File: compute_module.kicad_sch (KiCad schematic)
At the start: 4 parts

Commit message: Added annotated reference numbers
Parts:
- gave numbers to parts that had none: 4
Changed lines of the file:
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@@
   (symbol (lib_id "power:+3.3V") (at 195.58 60.96 0) (unit 1)
     (in_bom yes) (on_board yes)
-    (property "Reference" "#PWR?" (id 0) (at 195.58 64.77 0)
+    (property "Reference" "#PWR05" (id 0) (at 195.58 64.77 0)
       (effects (font (size 1.27 1.27)) hide)
     )
@@
   (symbol (lib_id "power:+3.3V") (at 215.9 46.99 0) (unit 1)
     (in_bom yes) (on_board yes)
-    (property "Reference" "#PWR?" (id 0) (at 215.9 50.8 0)
+    (property "Reference" "#PWR06" (id 0) (at 215.9 50.8 0)
       (effects (font (size 1.27 1.27)) hide)
     )
@@
   (symbol (lib_id "power:GND") (at 109.22 171.45 0) (unit 1)
     (in_bom yes) (on_board yes)
-    (property "Reference" "#PWR?" (id 0) (at 109.22 177.8 0)
+    (property "Reference" "#PWR04" (id 0) (at 109.22 177.8 0)
       (effects (font (size 1.27 1.27)) hide)
     )
@@
   (symbol (lib_id "power:GND") (at 215.9 82.55 0) (unit 1)
     (in_bom yes) (on_board yes)
-    (property "Reference" "#PWR?" (id 0) (at 215.9 88.9 0)
+    (property "Reference" "#PWR07" (id 0) (at 215.9 88.9 0)
       (effects (font (size 1.27 1.27)) hide)
     )
@@
   (symbol (lib_id "Device:R") (at 195.58 64.77 0) (unit 1)
     (in_bom yes) (on_board yes)
-    (property "Reference" "R?" (id 0) (at 197.3581 63.6206 0)
+    (property "Reference" "R4" (id 0) (at 197.3581 63.6206 0)
       (effects (font (size 1.27 1.27)) (justify left))
     )
@@
   (symbol (lib_id "Device:R") (at 208.28 72.39 90) (mirror x) (unit 1)
     (in_bom yes) (on_board yes)
-    (property "Reference" "R?" (id 0) (at 208.4006 75.4381 90)
+    (property "Reference" "R5" (id 0) (at 208.4006 75.4381 90)
       (effects (font (size 1.27 1.27)) (justify left))
     )
@@
   (symbol (lib_id "Connector:Micro_SD_Card_Det") (at 242.57 59.69 0) (unit 1)
     (in_bom yes) (on_board yes)
-    (property "Reference" "J?" (id 0) (at 241.3 38.9698 0))
+    (property "Reference" "J1" (id 0) (at 241.3 38.9698 0))
     (property "Value" "Micro_SD_Card_Det" (id 1) (at 241.3 41.2685 0))
     (property "Footprint" "" (id 2) (at 294.64 41.91 0)
@@
   (symbol (lib_id "symbols:ComputeModule4-CM4") (at 77.47 95.25 0) (unit 1)
     (in_bom yes) (on_board yes)
-    (property "Reference" "Module?" (id 0) (at 74.93 28.1494 0))
+    (property "Reference" "Module1" (id 0) (at 74.93 28.1494 0))
     (property "Value" "ComputeModule4-CM4" (id 1) (at 74.93 30.4481 0))
     (property "Footprint" "footprints:Raspberry-Pi-4-Compute-Module" (id 2) (at 219.71 121.92 0)

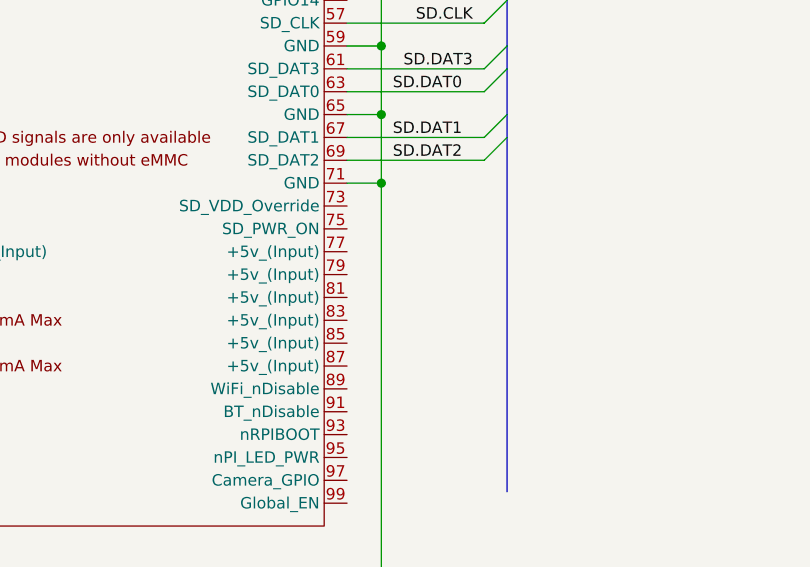
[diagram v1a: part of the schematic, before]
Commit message: visual tweaks to schematic
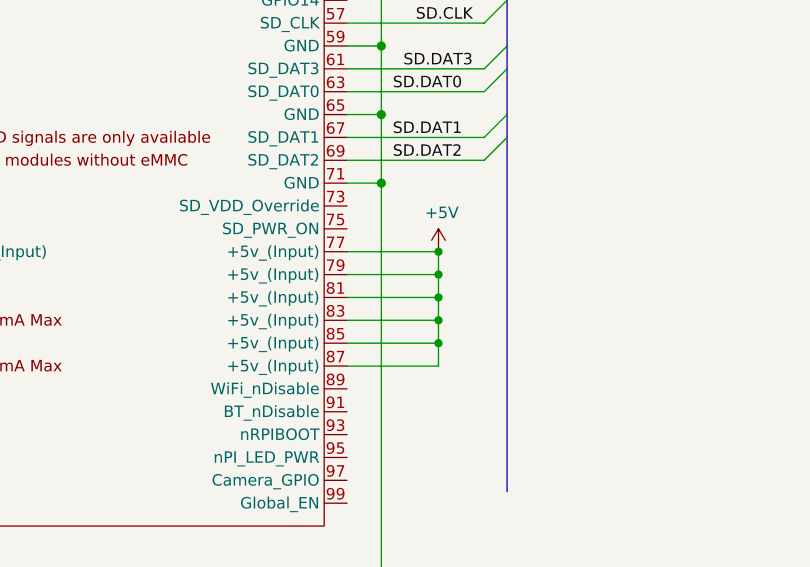
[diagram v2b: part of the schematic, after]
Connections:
- net +5V: now reaches Module1.77 (+5v_(Input))
- net +5V: now also Module1.79 (+5v_(Input)), Module1.81 (+5v_(Input)), Module1.83 (+5v_(Input)), Module1.85 (+5v_(Input)), Module1.87 (+5v_(Input))
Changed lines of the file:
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@@
   (junction (at 109.22 120.65) (diameter 1.016) (color 0 0 0 0))
   (junction (at 109.22 128.27) (diameter 1.016) (color 0 0 0 0))
+  (junction (at 115.57 135.89) (diameter 0.9144) (color 0 0 0 0))
+  (junction (at 115.57 138.43) (diameter 0.9144) (color 0 0 0 0))
+  (junction (at 115.57 140.97) (diameter 0.9144) (color 0 0 0 0))
+  (junction (at 115.57 143.51) (diameter 0.9144) (color 0 0 0 0))
+  (junction (at 115.57 146.05) (diameter 0.9144) (color 0 0 0 0))
   (junction (at 215.9 78.74) (diameter 1.016) (color 0 0 0 0))
   (bus_entry (at 123.19 107.95) (size -2.54 2.54)
@@
     (stroke (width 0) (type solid) (color 0 0 0 0))
   )
+  (wire (pts (xy 105.41 135.89) (xy 115.57 135.89))
+    (stroke (width 0) (type solid) (color 0 0 0 0))
+  )
+  (wire (pts (xy 105.41 138.43) (xy 115.57 138.43))
+    (stroke (width 0) (type solid) (color 0 0 0 0))
+  )
+  (wire (pts (xy 105.41 140.97) (xy 115.57 140.97))
+    (stroke (width 0) (type solid) (color 0 0 0 0))
+  )
+  (wire (pts (xy 105.41 143.51) (xy 115.57 143.51))
+    (stroke (width 0) (type solid) (color 0 0 0 0))
+  )
+  (wire (pts (xy 105.41 146.05) (xy 115.57 146.05))
+    (stroke (width 0) (type solid) (color 0 0 0 0))
+  )
   (wire (pts (xy 109.22 39.37) (xy 109.22 54.61))
     (stroke (width 0) (type solid) (color 0 0 0 0))
@@
   )
   (wire (pts (xy 109.22 128.27) (xy 109.22 171.45))
+    (stroke (width 0) (type solid) (color 0 0 0 0))
+  )
+  (wire (pts (xy 115.57 135.89) (xy 115.57 138.43))
+    (stroke (width 0) (type solid) (color 0 0 0 0))
+  )
+  (wire (pts (xy 115.57 138.43) (xy 115.57 140.97))
+    (stroke (width 0) (type solid) (color 0 0 0 0))
+  )
+  (wire (pts (xy 115.57 140.97) (xy 115.57 143.51))
+    (stroke (width 0) (type solid) (color 0 0 0 0))
+  )
+  (wire (pts (xy 115.57 143.51) (xy 115.57 146.05))
+    (stroke (width 0) (type solid) (color 0 0 0 0))
+  )
+  (wire (pts (xy 115.57 146.05) (xy 115.57 148.59))
+    (stroke (width 0) (type solid) (color 0 0 0 0))
+  )
+  (wire (pts (xy 115.57 148.59) (xy 105.41 148.59))
     (stroke (width 0) (type solid) (color 0 0 0 0))
   )
@@
     (effects (font (size 1.27 1.27)) (justify left bottom))
   )
+  (symbol (lib_id "power:+5V") (at 115.57 135.89 0) (unit 1)
+    (in_bom yes) (on_board yes)
+    (property "Reference" "#PWR?" (id 0) (at 115.57 139.7 0)
+      (effects (font (size 1.27 1.27)) hide)
+    )
+    (property "Value" "+5V" (id 1) (at 115.9383 131.5656 0))
+    (property "Footprint" "" (id 2) (at 115.57 135.89 0)
+      (effects (font (size 1.27 1.27)) hide)
+    )
+    (property "Datasheet" "" (id 3) (at 115.57 135.89 0)
+      (effects (font (size 1.27 1.27)) hide)
+    )
+  )
   (symbol (lib_id "power:+3.3V") (at 195.58 60.96 0) (unit 1)
